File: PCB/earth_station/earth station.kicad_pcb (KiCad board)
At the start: 2 copper layers, 50 x 50 mm, 9 parts, among them P1 CONN_01X02, U1 ARDUPROMINI, U2 RFM95, U3 LM2596_DC-DC

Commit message: Added Logos
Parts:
- added G***: LOGO, theinventorhouse:electronic_cats_logo_8x6, B.Cu at (144.9, 92.8)
- moved REF** 21.1 mm to (149.0, 89.2)
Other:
- board text added: "CatSat I"
- board text added: "Earth Station"

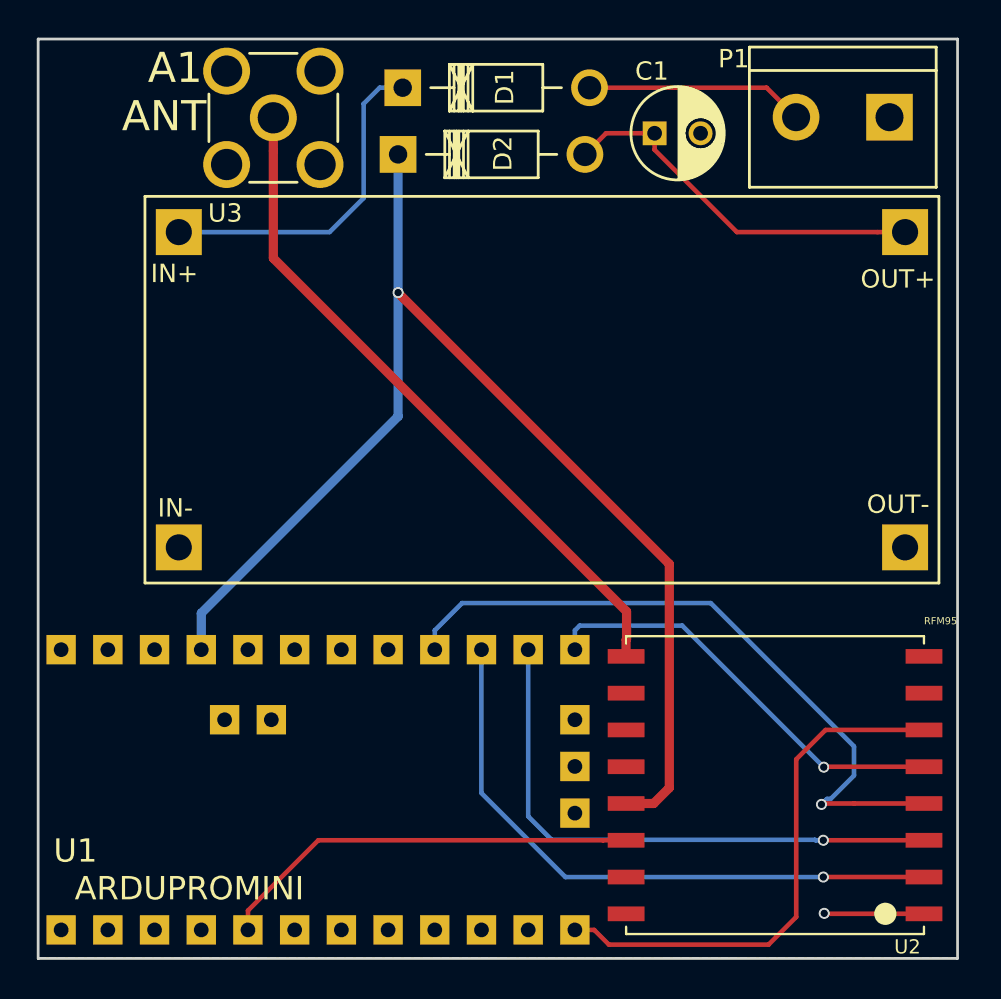
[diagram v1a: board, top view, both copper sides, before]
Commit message: Fix tracks and vias width
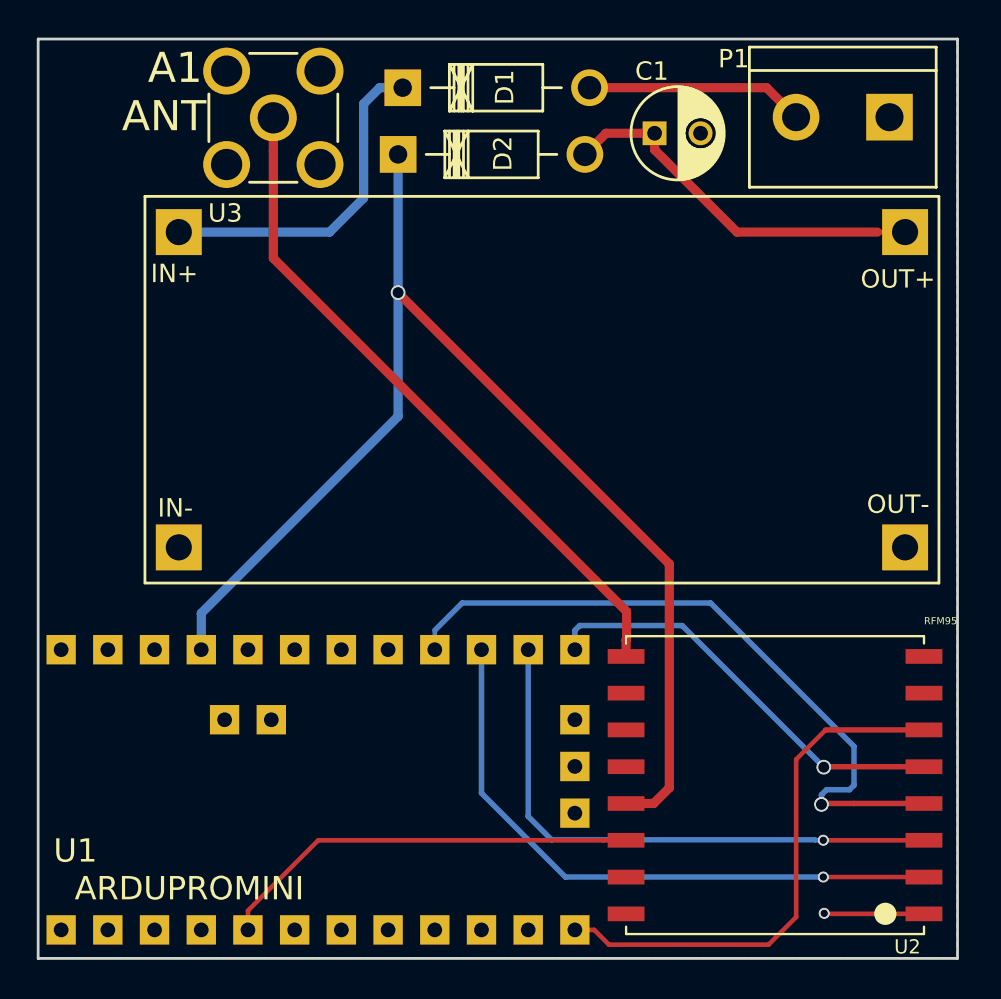
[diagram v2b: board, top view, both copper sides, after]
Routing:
- net /SCK: track 37.3 -> 37.9 mm
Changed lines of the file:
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@@
-(kicad_pcb (version 4) (host pcbnew 4.0.2+dfsg1-stable)
+(kicad_pcb (version 4) (host pcbnew 4.0.0-rc1-stable)
   (general
-    (links 0)
-    (no_connects 0)
-    (area 109.049999 72.599999 159.200001 122.750001)
+    (links 24)
+    (no_connects 11)
+    (area 109.049999 72.02246 162.627662 123.054432)
     (thickness 1.6)
     (drawings 6)
-    (tracks 74)
+    (tracks 75)
     (zones 0)
     (modules 10)
@@
   )
   (layers
-    (0 F.Cu signal hide)
-    (31 B.Cu signal hide)
+    (0 F.Cu signal)
+    (31 B.Cu signal)
     (32 B.Adhes user)
     (33 F.Adhes user)
@@
   (segment (start 143.45 101.225) (end 128.7 86.475) (width 0.5) (layer F.Cu) (net 3))
   (segment (start 128.7 86.475) (end 128.7 86.465349) (width 0.5) (layer F.Cu) (net 3))
-  (via (at 128.7 86.465349) (size 0.6) (drill 0.4) (layers F.Cu B.Cu) (net 3))
+  (via (at 128.7 86.465349) (size 0.8) (drill 0.6) (layers F.Cu B.Cu) (net 3))
   (segment (start 143.45 113.4) (end 143.45 101.225) (width 0.5) (layer F.Cu) (net 3))
   (segment (start 141.1 114.25) (end 142.6 114.25) (width 0.5) (layer F.Cu) (net 3))
@@
   (segment (start 124.36 116.25) (end 139.85 116.25) (width 0.25) (layer F.Cu) (net 7))
   (segment (start 150.35 111.85) (end 151.95 110.25) (width 0.25) (layer F.Cu) (net 14))
-  (segment (start 151.95 110.25) (end 157.3 110.25) (width 0.25) (layer F.Cu) (net 14))
+  (segment (start 151.95 110.25) (end 157.3 110.25) (width 0.3) (layer F.Cu) (net 14))
   (segment (start 150.35 120.425) (end 150.35 111.85) (width 0.25) (layer F.Cu) (net 14))
   (segment (start 148.85 121.925) (end 150.35 120.425) (width 0.25) (layer F.Cu) (net 14))
@@
   (segment (start 138.315 121.125) (end 139.365 121.125) (width 0.25) (layer F.Cu) (net 14))
   (segment (start 139.365 121.125) (end 140.165 121.925) (width 0.25) (layer F.Cu) (net 14))
-  (segment (start 152.224999 114.000001) (end 153.496082 112.728918) (width 0.25) (layer B.Cu) (net 22))
-  (segment (start 153.496082 112.728918) (end 153.496082 111.146082) (width 0.25) (layer B.Cu) (net 22))
-  (segment (start 151.725 114.3) (end 152.024999 114.000001) (width 0.25) (layer B.Cu) (net 22))
-  (segment (start 152.024999 114.000001) (end 152.224999 114.000001) (width 0.25) (layer B.Cu) (net 22))
-  (segment (start 153.496082 114.25) (end 151.775 114.25) (width 0.25) (layer F.Cu) (net 22))
+  (segment (start 151.725 114.3) (end 151.725 113.775) (width 0.3) (layer B.Cu) (net 22))
+  (segment (start 151.725 113.775) (end 152 113.5) (width 0.3) (layer B.Cu) (net 22))
+  (segment (start 130.695 104.835) (end 130.695 105.885) (width 0.25) (layer B.Cu) (net 22))
+  (segment (start 152 113.5) (end 153.25 113.5) (width 0.3) (layer B.Cu) (net 22))
+  (segment (start 153.25 113.5) (end 153.496082 113.253918) (width 0.3) (layer B.Cu) (net 22))
+  (segment (start 153.496082 113.253918) (end 153.496082 111.146082) (width 0.3) (layer B.Cu) (net 22))
+  (segment (start 153.496082 111.146082) (end 145.7 103.35) (width 0.3) (layer B.Cu) (net 22))
+  (segment (start 145.7 103.35) (end 132.18 103.35) (width 0.3) (layer B.Cu) (net 22))
+  (segment (start 132.18 103.35) (end 130.695 104.835) (width 0.3) (layer B.Cu) (net 22))
+  (segment (start 153.496082 114.25) (end 151.775 114.25) (width 0.3) (layer F.Cu) (net 22))
   (segment (start 151.775 114.25) (end 151.725 114.3) (width 0.25) (layer F.Cu) (net 22))
-  (via (at 151.725 114.3) (size 0.6) (drill 0.4) (layers F.Cu B.Cu) (net 22))
-  (segment (start 157.3 114.25) (end 153.496082 114.25) (width 0.25) (layer F.Cu) (net 22))
-  (segment (start 145.7 103.35) (end 153.496082 111.146082) (width 0.25) (layer B.Cu) (net 22))
-  (segment (start 132.18 103.35) (end 145.7 103.35) (width 0.25) (layer B.Cu) (net 22))
-  (segment (start 130.695 105.885) (end 130.695 104.835) (width 0.25) (layer B.Cu) (net 22))
-  (segment (start 130.695 104.835) (end 132.18 103.35) (width 0.25) (layer B.Cu) (net 22))
-  (segment (start 133.235 113.685) (end 137.8 118.25) (width 0.25) (layer B.Cu) (net 23))
-  (segment (start 137.8 118.25) (end 151.825 118.25) (width 0.25) (layer B.Cu) (net 23))
-  (segment (start 133.235 105.885) (end 133.235 113.685) (width 0.25) (layer B.Cu) (net 23))
+  (via (at 151.725 114.3) (size 0.8) (drill 0.6) (layers F.Cu B.Cu) (net 22))
+  (segment (start 157.3 114.25) (end 153.496082 114.25) (width 0.3) (layer F.Cu) (net 22))
+  (segment (start 133.235 113.685) (end 137.8 118.25) (width 0.3) (layer B.Cu) (net 23))
+  (segment (start 137.8 118.25) (end 151.825 118.25) (width 0.3) (layer B.Cu) (net 23))
+  (segment (start 133.235 105.885) (end 133.235 113.685) (width 0.3) (layer B.Cu) (net 23))
   (segment (start 157.3 118.25) (end 151.825 118.25) (width 0.25) (layer F.Cu) (net 23))
   (via (at 151.825 118.25) (size 0.6) (drill 0.4) (layers F.Cu B.Cu) (net 23))
-  (segment (start 137.05 116.225) (end 135.775 114.95) (width 0.25) (layer B.Cu) (net 24))
-  (segment (start 135.775 114.95) (end 135.775 105.885) (width 0.25) (layer B.Cu) (net 24))
-  (segment (start 151.375736 116.225) (end 137.05 116.225) (width 0.25) (layer B.Cu) (net 24))
+  (segment (start 137.05 116.225) (end 135.775 114.95) (width 0.3) (layer B.Cu) (net 24))
+  (segment (start 135.775 114.95) (end 135.775 105.885) (width 0.3) (layer B.Cu) (net 24))
+  (segment (start 151.375736 116.225) (end 137.05 116.225) (width 0.3) (layer B.Cu) (net 24))
   (segment (start 151.825 116.25) (end 151.400736 116.25) (width 0.25) (layer B.Cu) (net 24))
   (segment (start 151.400736 116.25) (end 151.375736 116.225) (width 0.25) (layer B.Cu) (net 24))
   (segment (start 157.3 116.25) (end 151.825 116.25) (width 0.25) (layer F.Cu) (net 24))
   (via (at 151.825 116.25) (size 0.6) (drill 0.4) (layers F.Cu B.Cu) (net 24))
-  (segment (start 151.85 112.275) (end 144.15 104.575) (width 0.25) (layer B.Cu) (net 25))
-  (segment (start 144.15 104.575) (end 138.575 104.575) (width 0.25) (layer B.Cu) (net 25))
-  (segment (start 138.575 104.575) (end 138.315 104.835) (width 0.25) (layer B.Cu) (net 25))
-  (segment (start 138.315 104.835) (end 138.315 105.885) (width 0.25) (layer B.Cu) (net 25))
-  (segment (start 157.3 112.25) (end 151.875 112.25) (width 0.25) (layer F.Cu) (net 25))
+  (segment (start 151.85 112.275) (end 144.15 104.575) (width 0.3) (layer B.Cu) (net 25))
+  (segment (start 144.15 104.575) (end 138.575 104.575) (width 0.3) (layer B.Cu) (net 25))
+  (segment (start 138.575 104.575) (end 138.315 104.835) (width 0.3) (layer B.Cu) (net 25))
+  (segment (start 138.315 104.835) (end 138.315 105.885) (width 0.3) (layer B.Cu) (net 25))
+  (segment (start 157.3 112.25) (end 151.875 112.25) (width 0.3) (layer F.Cu) (net 25))
   (segment (start 151.875 112.25) (end 151.85 112.275) (width 0.25) (layer F.Cu) (net 25))
-  (via (at 151.85 112.275) (size 0.6) (drill 0.4) (layers F.Cu B.Cu) (net 25))
-  (segment (start 142.65 77.8) (end 140.01 77.8) (width 0.25) (layer F.Cu) (net 33))
-  (segment (start 140.01 77.8) (end 138.86 78.95) (width 0.25) (layer F.Cu) (net 33))
-  (segment (start 142.65 78.7) (end 147.125 83.175) (width 0.25) (layer F.Cu) (net 33))
-  (segment (start 142.65 77.8) (end 142.65 78.7) (width 0.25) (layer F.Cu) (net 33))
-  (segment (start 147.125 83.175) (end 154.772 83.175) (width 0.25) (layer F.Cu) (net 33))
+  (via (at 151.85 112.275) (size 0.8) (drill 0.6) (layers F.Cu B.Cu) (net 25))
+  (segment (start 142.65 77.8) (end 140.01 77.8) (width 0.5) (layer F.Cu) (net 33))
+  (segment (start 140.01 77.8) (end 138.86 78.95) (width 0.5) (layer F.Cu) (net 33))
+  (segment (start 142.65 78.7) (end 147.125 83.175) (width 0.5) (layer F.Cu) (net 33))
+  (segment (start 142.65 77.8) (end 142.65 78.7) (width 0.5) (layer F.Cu) (net 33))
+  (segment (start 147.125 83.175) (end 154.772 83.175) (width 0.5) (layer F.Cu) (net 33))
   (segment (start 154.772 83.175) (end 156.272 83.175) (width 0.25) (layer F.Cu) (net 33))
-  (segment (start 148.74246 75.32246) (end 150.345 76.925) (width 0.25) (layer F.Cu) (net 34))
-  (segment (start 139.11 75.32246) (end 148.74246 75.32246) (width 0.25) (layer F.Cu) (net 34))
-  (segment (start 126.825 81.325) (end 126.825 76.19797) (width 0.25) (layer B.Cu) (net 35))
-  (segment (start 127.70051 75.32246) (end 128.95 75.32246) (width 0.25) (layer B.Cu) (net 35))
-  (segment (start 126.825 76.19797) (end 127.70051 75.32246) (width 0.25) (layer B.Cu) (net 35))
-  (segment (start 124.975 83.175) (end 126.825 81.325) (width 0.25) (layer B.Cu) (net 35))
-  (segment (start 116.775 83.175) (end 124.975 83.175) (width 0.25) (layer B.Cu) (net 35))
+  (segment (start 148.74246 75.32246) (end 150.345 76.925) (width 0.5) (layer F.Cu) (net 34))
+  (segment (start 139.11 75.32246) (end 148.74246 75.32246) (width 0.5) (layer F.Cu) (net 34))
+  (segment (start 126.825 81.325) (end 126.825 76.19797) (width 0.5) (layer B.Cu) (net 35))
+  (segment (start 127.70051 75.32246) (end 128.95 75.32246) (width 0.5) (layer B.Cu) (net 35))
+  (segment (start 126.825 76.19797) (end 127.70051 75.32246) (width 0.5) (layer B.Cu) (net 35))
+  (segment (start 124.975 83.175) (end 126.825 81.325) (width 0.5) (layer B.Cu) (net 35))
+  (segment (start 116.775 83.175) (end 124.975 83.175) (width 0.5) (layer B.Cu) (net 35))
   (zone (net 2) (net_name GND) (layer F.Cu) (hatch edge 0.508)
     (connect_pads (clearance 0.508))
